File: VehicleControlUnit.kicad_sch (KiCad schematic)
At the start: 6 parts, among them J3 Conn_01x02, Q1 Q_PMOS_GDS

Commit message: initial commit post VCU block diagram
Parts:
- added C8: 10u, Capacitor_SMD:C_0805_2012Metric, symbol Device:C
- added J10: Precharge_Ready, symbol Connector_Generic:Conn_01x02
- added J11, J12: Precharge+_Conn, symbol Connector_Generic:Conn_01x02
- added J5: MOTOR_CAN_IN, symbol Connector_Generic:Conn_01x04
- added J7: MOTOR_CAN_OUT, symbol Connector_Generic:Conn_01x04
- added J8, J9: CAR_CAN_IN, symbol Connector_Generic:Conn_01x02
- added LV1, LV2, LV3, LV4, LV5: LED, LED_SMD:LED_0805_2012Metric, symbol Device:LED
- added R19: 2k, Resistor_SMD:R_0805_2012Metric, symbol Device:R_US
- added R22: 30k, Resistor_SMD:R_0805_2012Metric, symbol Device:R_US
- added R23: 10k, symbol Device:R_US
- added R26, R27, R30, R31: 1k, Resistor_SMD:R_0805_2012Metric, symbol Device:R_US
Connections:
- net LV+: now also C8.1, J10.1 (Pin_1), J5.1 (Pin_1), J7.1 (Pin_1), R19.1
- net LVGND renamed GND
- net GND: now also C8.2, J5.2 (Pin_2), J7.2 (Pin_2), LV1.1 (K), LV2.1 (K), LV3.1 (K), LV4.1 (K), LV5.1 (K), R23.2
- new net: LV4.2 (A), R30.2
- new net: LV2.2 (A), R26.2
- new net: J10.2 (Pin_2), R22.1
- new net: LV5.2 (A), R31.2
- new net: LV3.2 (A), R27.2
- new net: LV1.2 (A), R19.2
- new net CAN_H: J5.3 (Pin_3), J7.3 (Pin_3), J8.1 (Pin_1), J9.1 (Pin_1)
- new net CAN_L: J5.4 (Pin_4), J7.4 (Pin_4), J8.2 (Pin_2), J9.2 (Pin_2)
- new net ISO_ADC_CLK: J11.2 (Pin_2), J12.2 (Pin_2)
- new net Precharge_Ready: R22.2, R23.1
- new net VPrecharge+: J11.1 (Pin_1)
- new net VPrecharge-: J12.1 (Pin_1)
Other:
- removed sheet ActivePrecharge
- removed sheet CAN
- removed sheet HVArchitecture
- removed sheet PowerMisc
- added sheet ESP (ESP.kicad_sch)
- sheet ContactorDriver ports: added none; removed APre_Enable, APre_Sense, LVGND
- note added: "12V Input Bypass Cap"
- note added: "From Optocoupler on Precharge Board"
- note added: "LV PWR indicator LED"
- note added: "VPrecharge+/- ISO ADC data signals from precharge board Prob AMC1305M25 ISO ADC"
- moved on the sheet: 12V_TP1, D1, J3, LVGND_TP1, Q1, R11

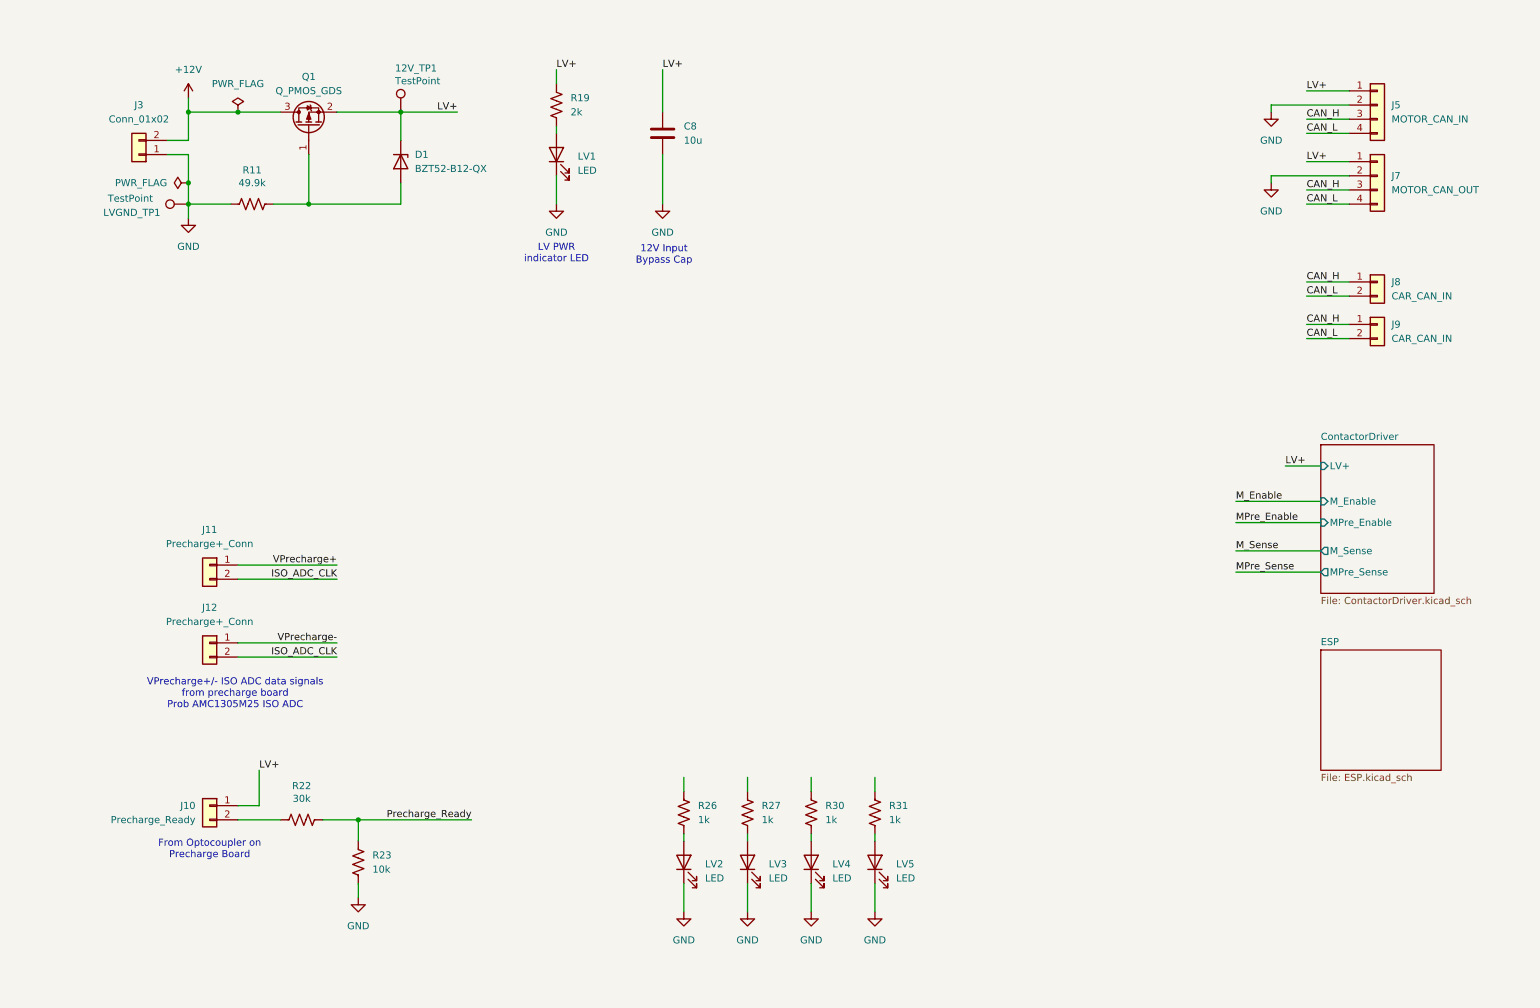
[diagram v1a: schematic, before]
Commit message: sch for review missing LSOM
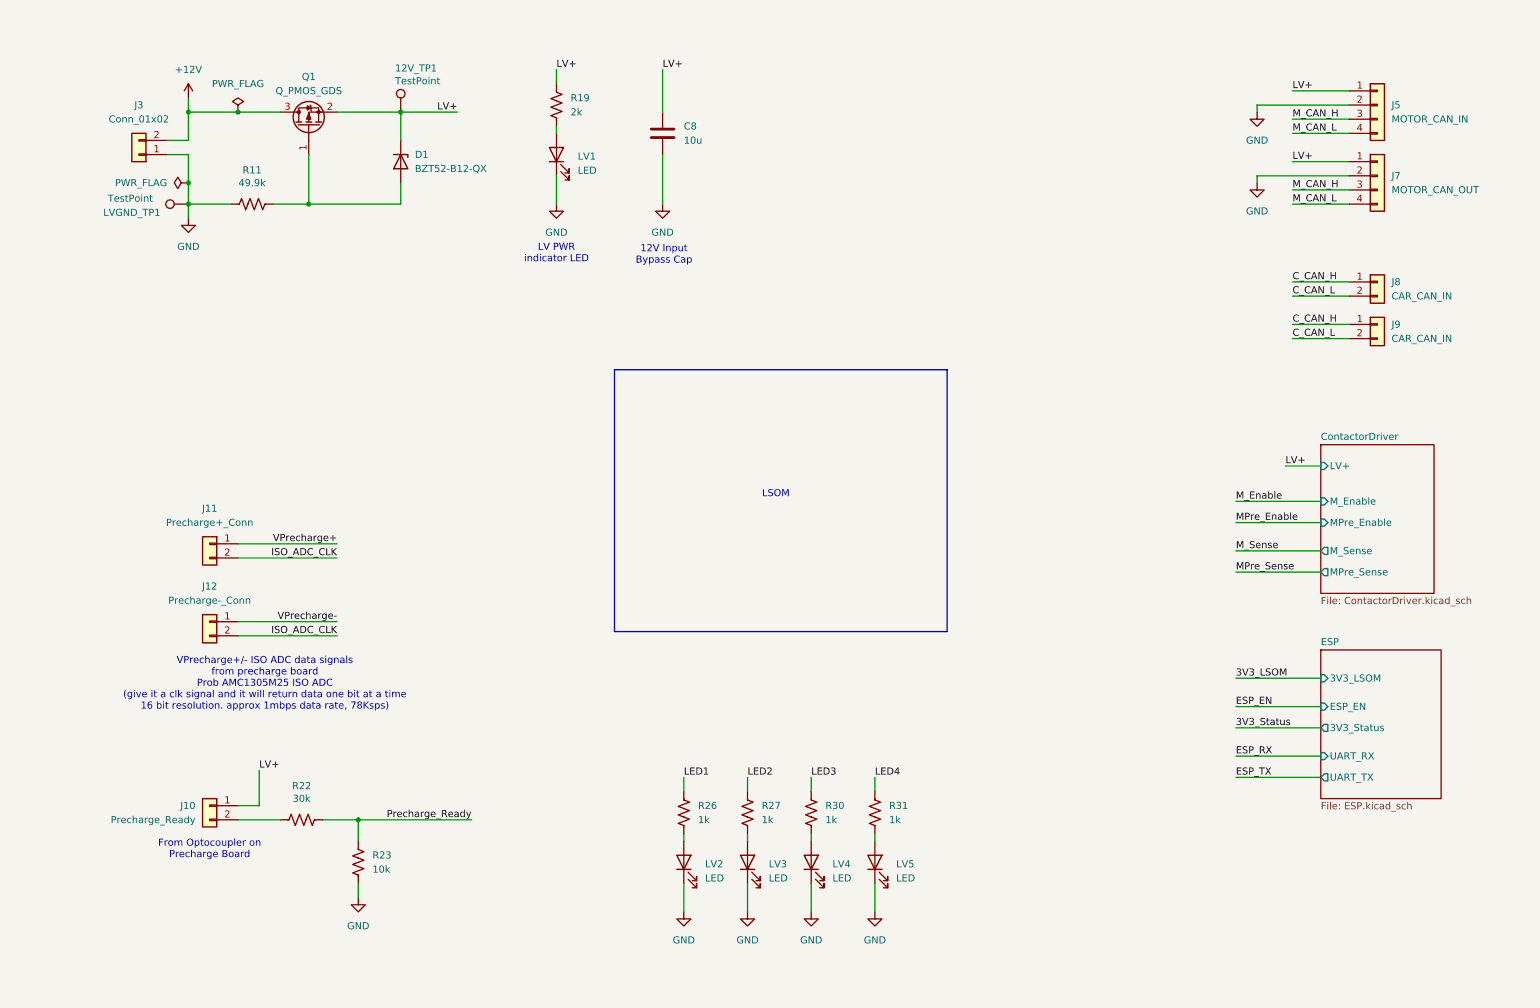
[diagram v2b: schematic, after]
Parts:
- J12: value Precharge+_Conn -> Precharge-_Conn
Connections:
- net LED1: now reaches R26.1
- net LED3: now reaches R30.1
- net LED4: now reaches R31.1
- net LED2: now reaches R27.1
- net CAN_H renamed C_CAN_H
- net C_CAN_H: no longer J5.3 (Pin_3), J7.3 (Pin_3)
- net CAN_L renamed C_CAN_L
- net C_CAN_L: no longer J5.4 (Pin_4), J7.4 (Pin_4)
- new net M_CAN_H: J5.3 (Pin_3), J7.3 (Pin_3)
- new net M_CAN_L: J5.4 (Pin_4), J7.4 (Pin_4)
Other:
- sheet ESP ports: added 3V3_LSOM, 3V3_Status, ESP_EN, UART_RX, UART_TX; removed none
- note added: "LSOM"
- note added: "VPrecharge+/- ISO ADC data signals from precharge board Prob AMC1305M25 ISO ADC (give it a clk signal and it will return data one bit at a time 16 bit resolution. approx 1mbps data rate, 78Ksps)"
- note removed: "VPrecharge+/- ISO ADC data signals from precharge board Prob AMC1305M25 ISO ADC"
- moved on the sheet: J11, J12

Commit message: add lsom sym
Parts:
- added J2: ~, symbol utsvt-conn:LSOM_DaughterConn
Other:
- note removed: "LSOM"

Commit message: pOSPAOBJCO
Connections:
- net 3V3_LSOM: now also J2.1 (+3.3V), J2.2 (+3.3V), J2.3 (+3.3V), J2.4 (+3.3V), J2.45 (+3.3V), J2.46 (+3.3V), J2.47 (+3.3V), J2.48 (+3.3V)
- net C_CAN_H: now also J2.30 (CCAN_H)
- net C_CAN_L: now also J2.32 (CCAN_L)
- net GND: now also J2.10 (GND), J2.12 (GND), J2.13 (GND), J2.15 (GND), J2.25 (GND), J2.26 (GND), J2.27 (GND), J2.28 (GND), J2.29 (GND), J2.38 (GND), J2.40 (GND)
- net LV+: now also J2.21 (12VExt), J2.22 (12VExt), J2.23 (12VExt), J2.24 (12VExt)
- net M_CAN_H: now also J2.6 (ICAN_H)
- net M_CAN_L: now also J2.8 (ICAN_L)
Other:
- moved on the sheet: J10, J11, J12, J2A, J2B, R22, R23

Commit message: review LSOM
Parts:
- added C13: 10n, Capacitor_SMD:C_0805_2012Metric, symbol Device:C
- J2: footprint (none) -> UTSVT_Special:LeaderSOM
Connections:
- net 3V3_LSOM: now also J2.37 (+3.3VA), J2.39 (+3.3VA)
- net ESP_EN: now also J2.31 (ADC1_IN10)
- net ESP_RX: now also J2.19 (UART5_RX)
- net ESP_TX: now also J2.17 (UART5_TX)
- net GND: now also J2.33 (GNDA), J2.34 (GNDA), J2.35 (GNDA), J2.36 (GNDA), C13.2
- net ISO_ADC_CLK: now also J2.20 (SPI2_SCK)
- net LED1: now also J2.43 (ADC1_IN12)
- net LED2: now also J2.41 (ADC1_IN11)
- net LED3: now also J2.44 (ADC1_IN3)
- net LED4: now also J2.42 (ADC1_IN2)
- net MPre_Enable: now also J2.9 (I2C3_SDA)
- net MPre_Sense: now also J2.5 (I2C1_SDA)
- net M_Enable: now also J2.11 (I2C3_SCL)
- net M_Sense: now also J2.7 (I2C1_SCL)
- net Precharge_Ready: now also J2.14 (SPI2_MISO), C13.1
- net VPrecharge+: now also J2.18 (SPI2_MOSI)
- net VPrecharge-: now also J2.16 (SPI2_CS)
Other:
- sheet ESP ports: added none; removed 3V3_Status
- note added: "CAN Connectors"
- note added: "Debug LEDs"
- note added: "LSOM"
- note added: "Power"
- note added: "Precharge Connectors"
- note added: "VPrecharge+/- ISO ADC data signals from precharge board Prob AMC1305M25 ISO ADC (give it a clk signal from LSOM and it will return data one bit at a time 16 bit resolution. approx 1mbps data rate, 78Ksps)"
- note added: "can make ESP enabled all the time to save an LSOM pin"
- note added: "lowpass filter Fc = 530hz"
- note removed: "VPrecharge+/- ISO ADC data signals from precharge board Prob AMC1305M25 ISO ADC (give it a clk signal and it will return data one bit at a time 16 bit resolution. approx 1mbps data rate, 78Ksps)"
- moved on the sheet: J10, J11, J12, J2A, J2B, J5, J7, J8, J9, LV2, LV3, LV4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

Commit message: review sch one last time
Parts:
- removed R22: 30k, Resistor_SMD:R_0805_2012Metric, symbol Device:R_US
- added J15: CAR_CAN_Breakout, symbol Connector_Generic:Conn_01x02
- added J16: MOTOR_CAN_Breakout, symbol Connector_Generic:Conn_01x02
- added R34: 100, symbol Device:R_US
- C13: value 10n -> 1u
- J9: value CAR_CAN_IN -> CAR_CAN_OUT
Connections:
- net 3V3_LSOM: now also J10.1 (Pin_1); no longer J2.37 (+3.3VA), J2.39 (+3.3VA)
- net C_CAN_H: now also J15.1 (Pin_1)
- net C_CAN_L: now also J15.2 (Pin_2)
- net ESP_RX: now also J2.17 (UART5_TX); no longer J2.19 (UART5_RX)
- net ESP_TX: now also J2.19 (UART5_RX); no longer J2.17 (UART5_TX)
- net LV+: no longer J10.1 (Pin_1)
- net M_CAN_H: now also J16.1 (Pin_1)
- net M_CAN_L: now also J16.2 (Pin_2)
- net Precharge_Ready: now also R34.2
- net at J10.2 (Pin_2): now also R34.1
- net ESP_EN: no longer names the net of J2.31 (ADC1_IN10)
- no-connect marks 0 -> 3
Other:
- sheet ESP ports: added none; removed ESP_EN
- note added: "Lowpass Filter Fc = 1.6kHz"
- note removed: "lowpass filter Fc = 530hz"
- moved on the sheet: J5, J7, J8, J9

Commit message: added opto's to sense signals
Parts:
- R23, R34: footprint (none) -> Resistor_SMD:R_0805_2012Metric
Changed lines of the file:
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@@
 			)
 		)
-		(property "Footprint" ""
+		(property "Footprint" "Resistor_SMD:R_0805_2012Metric"
 			(at 59.944 165.354 90)
 			(effects
@@
 			)
 		)
-		(property "Footprint" ""
+		(property "Footprint" "Resistor_SMD:R_0805_2012Metric"
 			(at 70.866 174.244 90)
 			(effects

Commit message: layout start
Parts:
- added H1, H2, H3: MountingHole, MountingHole:MountingHole_3.2mm_M3, symbol Mechanical:MountingHole
- 12V_TP1, LVGND_TP1: footprint utsvt-special:TestPoint_HEX_3mmID -> UTSVT_Special:TestPoint_HEX_3mmID
- J1: renamed from J3; footprint utsvt-conn:Molex_MicroFit3.0_1x2xP3.00mm_PolarizingPeg_Vertical -> utsvt_conn:Molex_MicroFit3.0_1x2xP3.00mm_PolarizingPeg_Vertical
- J10: renamed from J9; footprint (none) -> utsvt_conn:Molex_MicroFit3.0_1x2xP3.00mm_PolarizingPeg_Vertical
- J11: renamed from J15; footprint (none) -> Connector_PinHeader_2.54mm:PinHeader_1x02_P2.54mm_Vertical
- J2: renamed from J10; footprint (none) -> utsvt_conn:Molex_MicroFit3.0_1x2xP3.00mm_PolarizingPeg_Vertical
- J4: renamed from J11; footprint (none) -> utsvt_conn:Molex_MicroFit3.0_1x2xP3.00mm_PolarizingPeg_Vertical
- J5: renamed from J12; footprint (none) -> utsvt_conn:Molex_MicroFit3.0_1x2xP3.00mm_PolarizingPeg_Vertical
- J6: renamed from J5; footprint (none) -> utsvt_conn:Molex_MicroFit3.0_1x4xP3.00mm_PolarizingPeg_Vertical
- J7: footprint (none) -> utsvt_conn:Molex_MicroFit3.0_1x4xP3.00mm_PolarizingPeg_Vertical
- J8: renamed from J16; footprint (none) -> Connector_PinHeader_2.54mm:PinHeader_1x02_P2.54mm_Vertical
- J9: renamed from J8; footprint (none) -> utsvt_conn:Molex_MicroFit3.0_1x2xP3.00mm_PolarizingPeg_Vertical
- renumbered C13 to C1, C8 to C2, J2 to J3, R11 to R1, R34 to R2, R23 to R3, R19 to R4, R26 to R5, R27 to R6, R30 to R7, R31 to R8
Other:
- sheet ContactorDriver ports: added 3V3_LSOM, LVGND; removed none
